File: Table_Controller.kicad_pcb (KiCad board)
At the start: 4 copper layers, 103.1 x 50 mm, 96 parts, among them J1 Dell DC jack, J11 HX JN1.27-2x5 WZ H4.9, J12 JST B4B XH A, J13 Conn_01x14_Pin, J14 JST B6B XH A, J15 2.54 mm header, J2 USB_C_Receptacle_USB2.0_16P, J3 DC barrel assy, U1 USBLC6-2SC6, U10 STM32G431K8Tx, U11 LMR380x0, U12 VNH7070, Y10 20 MHz

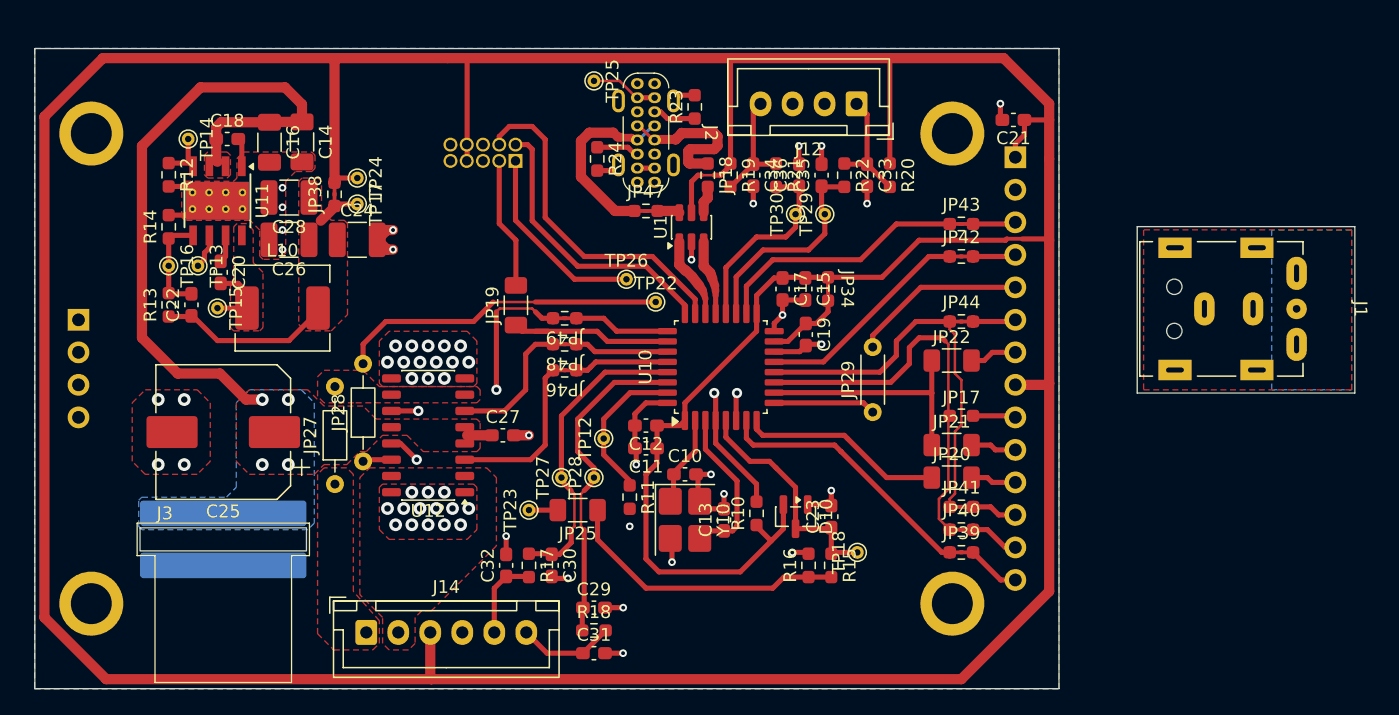
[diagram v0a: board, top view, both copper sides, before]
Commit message: top silk done
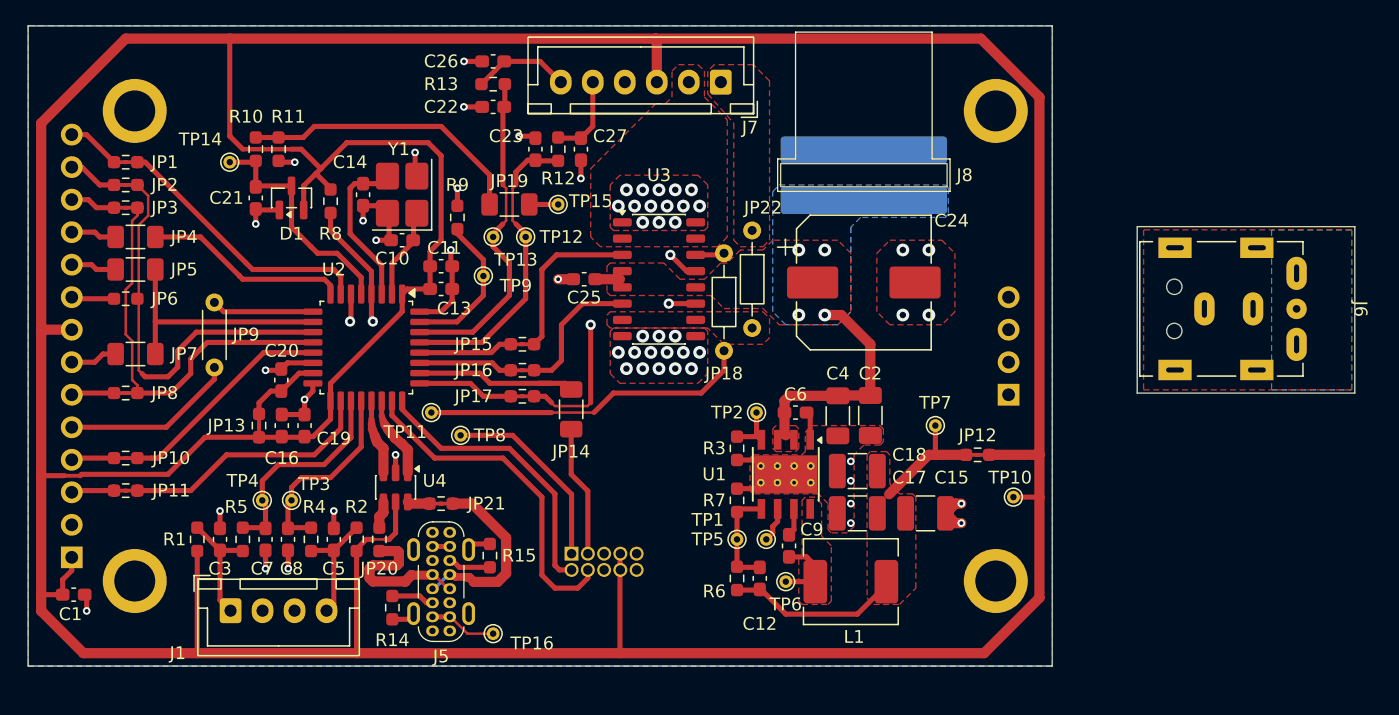
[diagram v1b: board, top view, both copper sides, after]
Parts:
- moved C1 82.2 mm to (18.0, 57.7), turned to 0 degrees
- moved J3 80.1 mm to (17.9, 54.7), turned to 0 degrees
- moved J2 72.9 mm to (91.1, 42.0), turned to 0 degrees
- moved JP1 72.0 mm to (22.1, 23.9), turned to 180 degrees
- moved JP2 70.6 mm to (22.1, 25.7), turned to 180 degrees
- moved JP3 69.3 mm to (22.1, 27.4), turned to 180 degrees
- moved JP11 68.5 mm to (22.1, 49.5), turned to 180 degrees
- moved JP10 67.2 mm to (22.1, 47.0), turned to 180 degrees
- moved JP4 66.5 mm to (22.9, 29.7), turned to 180 degrees
- moved JP6 65.9 mm to (22.1, 34.5), turned to 180 degrees
- moved JP8 65.5 mm to (22.1, 41.9), turned to 180 degrees
- moved JP5 65.2 mm to (22.9, 32.3), turned to 180 degrees
- moved JP7 63.8 mm to (22.9, 38.9), turned to 180 degrees
- moved J1 62.9 mm to (30.3, 58.9), turned to 0 degrees
- moved R1 61.1 mm to (27.7, 53.3), turned to 90 degrees
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- renumbered C21 to C1, C22 to C12, C12 to C13, C13 to C14, C24 to C15, C15 to C16, C26 to C17, C28 to C18, C17 to C19, C14 to C2, C19 to C20, C23 to C21, C29 to C22, C30 to C23, C25 to C24, C27 to C25, C31 to C26, C32 to C27, C33 to C3, C16 to C4, C34 to C5, C18 to C6, C35 to C7, C36 to C8, C20 to C9, D10 to D1, J12 to J1, J15 to J2, J13 to J3, J11 to J4, J2 to J5, J1 to J6, J14 to J7, J3 to J8, JP39 to JP1, JP42 to JP10, JP43 to JP11, JP38 to JP12, JP34 to JP13, JP19 to JP14, JP46 to JP15, JP48 to JP16, JP49 to JP17, JP28 to JP18, JP25 to JP19, JP40 to JP2, JP18 to JP20, JP47 to JP21, JP27 to JP22, JP41 to JP3, JP20 to JP4, JP21 to JP5, JP17 to JP6, JP22 to JP7, JP44 to JP8, JP29 to JP9, L10 to L1, R20 to R1, R15 to R10, R16 to R11, R17 to R12, R18 to R13, R23 to R14, R24 to R15, R19 to R2, R12 to R3, R21 to R4, R22 to R5, R13 to R6, R14 to R7, R10 to R8, R11 to R9, TFT10 to TFT1, TP13 to TP1, TP24 to TP10, TP22 to TP11, TP27 to TP12, TP28 to TP13, TP18 to TP14, TP23 to TP15, TP25 to TP16, TP14 to TP2, TP30 to TP3, TP29 to TP4, TP16 to TP5, TP15 to TP6, TP17 to TP7, TP26 to TP8, TP12 to TP9, U11 to U1, U10 to U2, U12 to U3, U1 to U4, Y10 to Y1
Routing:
- net /S19V5: track 54.2 -> 20.0 mm
- net /S3V3: track 362.6 -> 369.3 mm
- net /3V3_REG: track 17.8 -> 23.9 mm
- net /GND: track 56.8 -> 58.2 mm
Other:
- board size 103.1 x 50 mm -> 103.6 x 50 mm

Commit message: layout ready for mfg review
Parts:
- added TP17: TestPoint, TestPoint:TestPoint_THTPad_D1.0mm_Drill0.5mm, F.Cu at (29.5, 49.0)
- added TP18: TestPoint, TestPoint:TestPoint_THTPad_D1.0mm_Drill0.5mm, F.Cu at (91.4, 52.3)
- added TP19: TestPoint, TestPoint:TestPoint_THTPad_D1.0mm_Drill0.5mm, F.Cu at (30.2, 26.4)
- added TP20: TestPoint, TestPoint:TestPoint_THTPad_D1.0mm_Drill0.5mm, F.Cu at (73.4, 60.5)
- added TP21: TestPoint, TestPoint:TestPoint_THTPad_D1.0mm_Drill0.5mm, F.Cu at (55.9, 29.5)
- moved J6 27.9 mm to (102.4, 63.2), turned to 0 degrees
- moved TP9 1.02 mm to (50.0, 33.8)
- moved J8 0.25 mm to (79.8, 24.6)
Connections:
- J8 pad 2: (no net) -> /GND
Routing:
- net /GND: vias 58 -> 62
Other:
- board size 103.6 x 50 mm -> 94.2 x 50 mm
- board text added: "23/09/2026"
- board text added: "3V3_REG"
- board text added: "BOT"
- board text added: "CS"
- board text added: "ENCa"
- board text added: "ENCb"
- board text added: "Felipe L Rodrigues"
- board text added: "Limit sw"
- board text added: "MOT_CS"
- board text added: "Mini display"
- board text added: "Motor"
- board text added: "PWR in"
- board text added: "S3V3"
- board text added: "TOP"
- board text added: "Table controller"

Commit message: added aux board for cable extension
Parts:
- added J10: JST B6B XH A, Connector_JST:JST_XH_B6B-XH-A_1x06_P2.50mm_Vertical, B.Cu at (99.3, 32.3)
- added J9: JST B6B XH A, Connector_JST:JST_XH_B6B-XH-A_1x06_P2.50mm_Vertical, F.Cu at (105.4, 32.3)
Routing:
- net Net-(J10-Pin_6): track 0.00 -> 6.10 mm
- net Net-(J10-Pin_5): track 0.00 -> 6.10 mm
- net Net-(J10-Pin_4): track 0.00 -> 6.10 mm
- net Net-(J10-Pin_3): track 0.00 -> 6.10 mm
- net Net-(J10-Pin_2): track 0.00 -> 6.10 mm
- net Net-(J10-Pin_1): track 0.00 -> 6.10 mm
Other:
- board text added: "Disp. ext."
- board text removed: "Mini display"
